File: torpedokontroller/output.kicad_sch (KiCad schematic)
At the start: 17 parts, among them IC9 TCAN3414DR, Q6 PMOS, Q8 STANDARD_140356145200, U3 TPS26400PWP

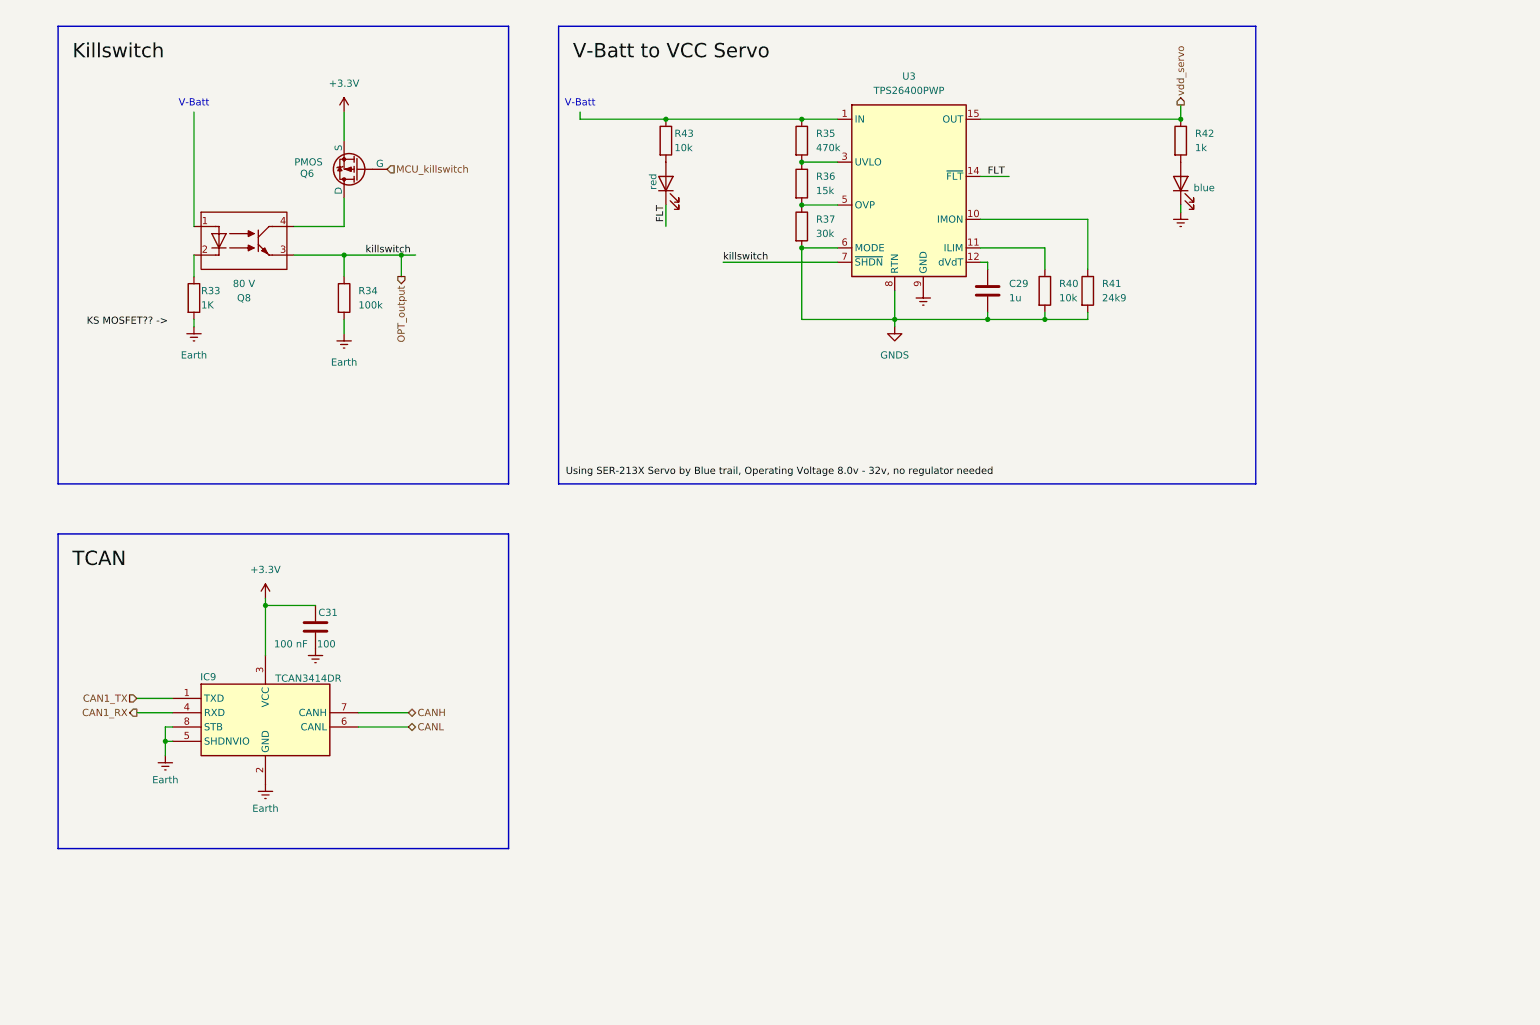
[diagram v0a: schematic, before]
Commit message: v0.5
USB2.0 implemented fr
many other things
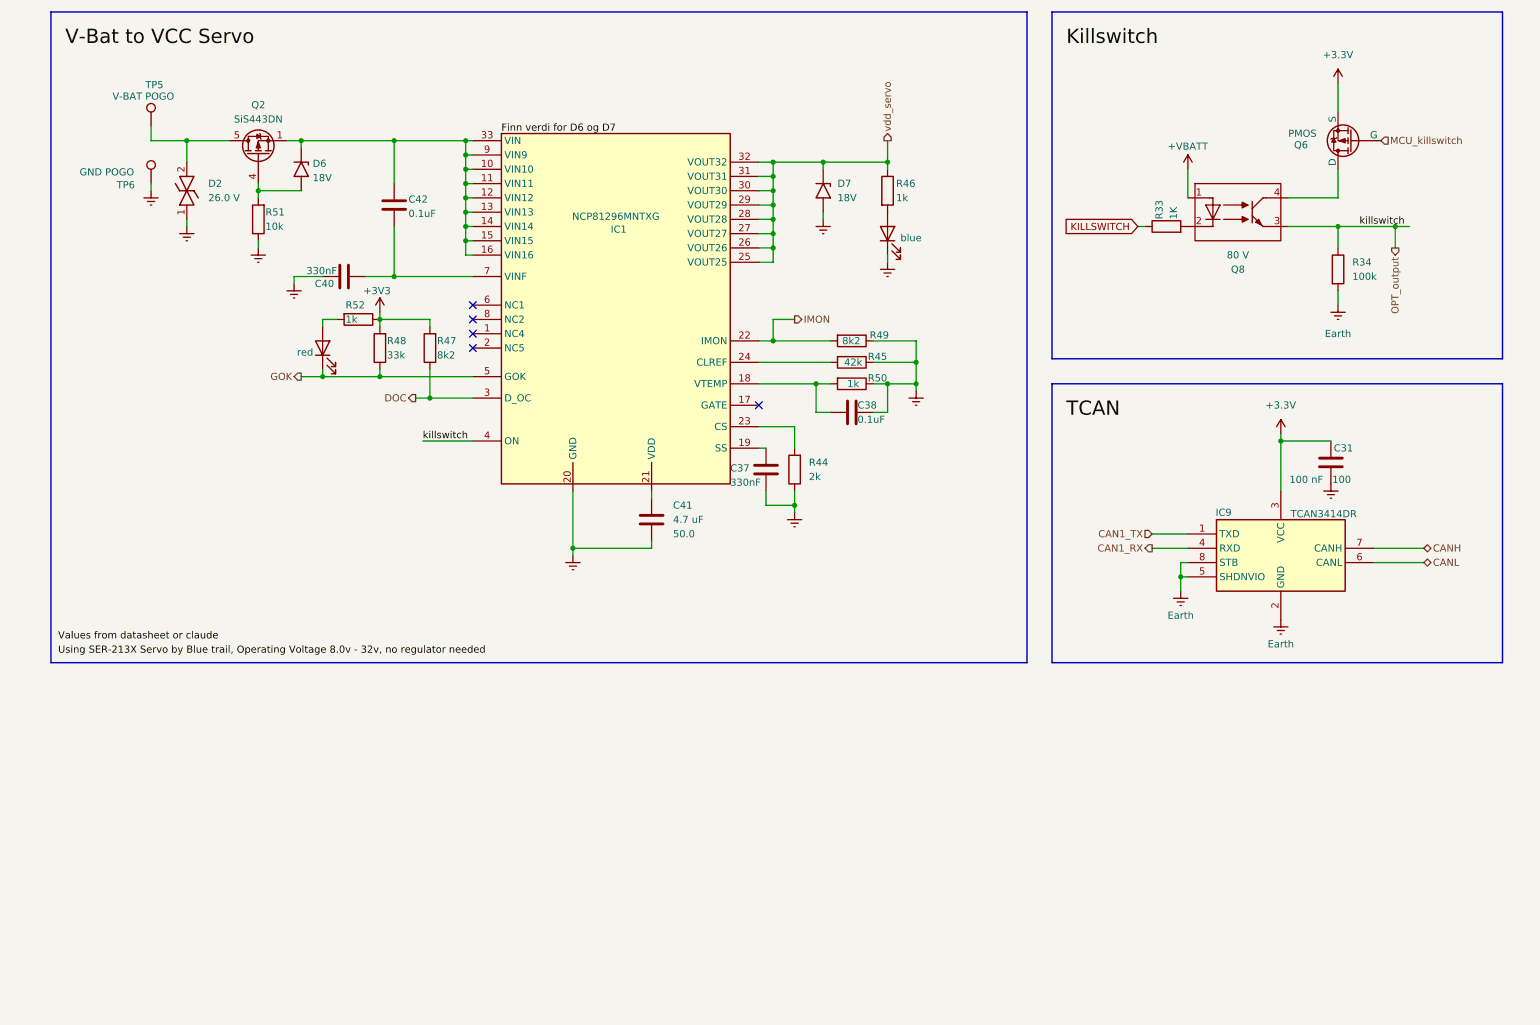
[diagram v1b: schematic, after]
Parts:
- removed C29: 1u, symbol Device:C
- removed D14: blue, symbol Device:LED
- removed D15: red, symbol Device:LED
- removed R35: 470k, symbol Device:R
- removed R36: 15k, symbol Device:R
- removed R37: 30k, symbol Device:R
- removed R40, R43: 10k, symbol Device:R
- removed R41: 24k9, symbol Device:R
- removed R42: 1k, symbol Device:R
- removed U3: TPS26400PWP, Package_SO:HTSSOP-16-1EP_4.4x5mm_P0.65mm_EP3.4x5mm_Mask2.66x2.46mm_ThermalVias, symbol Power_Management:TPS26400PWP
- added C37, C40: 330nF, symbol Device:C
- added C38, C42: 0.1uF, symbol Device:C
- added C41: 4.7 uF, Capacitor_SMD_Wurth:C_Wurth_WCAP-CSGP-1210_H2.5, symbol Capacitor_Wurth_WCAP-CSGP:1210_H2.5_885012209048
- added D16: blue, symbol Device:LED
- added D17: red, symbol Device:LED
- added D2: DO214-AA-600W_BI_824521261, Diode_SMD_Wurth:D_Wurth_WE-TVSP-DO214-AA-600W_BI, symbol WE-TVSP:DO214-AA-600W_BI_824521261
- added D6, D7: 18V, Diode_SMD:D_SMA, symbol Diode:SMAJ18A
- added IC1: NCP81296MNTXG, QFN50P500X500X140-33N, symbol efuse_big:NCP81296MNTXG
- added Q2: SiS443DN, Package_SO:Vishay_PowerPAK_1212-8_Single, symbol Transistor_FET:SiS443DN
- added R44: 2k, symbol Device:R
- added R45: 42k, symbol Device:R
- added R46, R50, R52: 1k, symbol Device:R
- added R47, R49: 8k2, symbol Device:R
- added R48: 33k, symbol Device:R
- added R51: 10k, symbol Device:R
- added TP5: V-BAT POGO, Optocoupler_SMD_Wurth:Q_Wurth_WL-OCPT_SOP4-STANDARD, symbol Connector:TestPoint
- added TP6: GND POGO, Optocoupler_SMD_Wurth:Q_Wurth_WL-OCPT_SOP4-STANDARD, symbol Connector:TestPoint
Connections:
- net Earth: now also C37.2, C38.1, C40.1, C41.2, D16.1 (K), D2.1, D7.2 (A2), IC1.20 (GND), R44.1, R45.1, R49.1, R50.1, R51.1, TP6.1; no longer R33.2
- net OPT_output: now also IC1.4 (ON)
- net vdd_servo: now also D7.1 (A1), IC1.25 (VOUT25), IC1.26 (VOUT26), IC1.27 (VOUT27), IC1.28 (VOUT28), IC1.29 (VOUT29), IC1.30 (VOUT30), IC1.31 (VOUT31), IC1.32 (VOUT32), R46.1
- net +VBATT: now reaches Q8.1 (A)
- net at Q8.2 (C): now also R33.2; no longer R33.1
- new net: IC1.24 (CLREF), R45.2
- new net: D17.2 (A), R52.2
- new net: IC1.23 (CS), R44.2
- new net: C42.2, D6.1 (A1), IC1.10 (VIN10), IC1.11 (VIN11), IC1.12 (VIN12), IC1.13 (VIN13), IC1.14 (VIN14), IC1.15 (VIN15), IC1.16 (VIN16), IC1.33 (VIN), IC1.9 (VIN9), Q2.1 (S), Q2.2 (S), Q2.3 (S)
- new net: D6.2 (A2), Q2.4 (G), R51.2
- new net: D2.2, Q2.5 (D), TP5.1
- new net: D16.2 (A), R46.2
- new net: C41.1, IC1.21 (VDD)
- new net: C37.1, IC1.19 (SS)
- new net: C38.2, IC1.18 (VTEMP), R50.2
- new net: C40.2, C42.1, IC1.7 (VINF)
- new net +3V3: R47.2, R48.2, R52.1
- new net DOC: IC1.3 (D_OC), R47.1
- new net GOK: D17.1 (K), IC1.5 (GOK), R48.1
- new net IMON: IC1.22 (IMON), R49.2
- new net KILLSWITCH: R33.1
- no-connect marks 0 -> 5
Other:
- note removed: "V-Batt"
- moved on the sheet: C31, IC9, Q6, Q8, R33, R34

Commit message: v 0.6
New MCU package
Added SWD, Rest and boot
Moved USB2.0 to MCU page
Other small changes
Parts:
- R49: value 8k2 -> 2k
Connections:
- net DOC renamed D_OC
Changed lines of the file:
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@@
 	(paper "A4")
 	(title_block
-		(date "2026-10-03")
+		(date "2026-10-07")
 		(comment 1 "Simon Torvund")
 	)
@@
 	)
 	(junction
-		(at 146.05 74.93)
+		(at 147.32 74.93)
 		(diameter 0)
 		(color 0 0 0 0)
@@
 	(wire
 		(pts
-			(xy 143.51 74.93) (xy 146.05 74.93)
+			(xy 143.51 74.93) (xy 156.21 74.93)
 		)
 		(stroke
@@
 	(wire
 		(pts
-			(xy 149.86 104.14) (xy 149.86 105.41)
+			(xy 149.86 104.14) (xy 149.86 113.03)
 		)
 		(stroke
@@
 	(wire
 		(pts
-			(xy 146.05 71.12) (xy 149.86 71.12)
+			(xy 147.32 71.12) (xy 151.13 71.12)
 		)
 		(stroke
@@
 	(wire
 		(pts
-			(xy 146.05 74.93) (xy 156.21 74.93)
-		)
-		(stroke
-			(width 0)
-			(type default)
-		)
-	)
-	(wire
-		(pts
 			(xy 166.37 59.69) (xy 166.37 60.96)
 		)
@@
 	(wire
 		(pts
-			(xy 41.91 53.34) (xy 41.91 54.61)
-		)
-		(stroke
-			(width 0)
-			(type default)
-		)
-	)
-	(wire
-		(pts
 			(xy 91.44 41.91) (xy 92.71 41.91)
 		)
@@
 	(wire
 		(pts
-			(xy 146.05 71.12) (xy 146.05 74.93)
+			(xy 147.32 71.12) (xy 147.32 74.93)
 		)
 		(stroke
@@
 	(wire
 		(pts
+			(xy 41.91 53.34) (xy 41.91 58.42)
+		)
+		(stroke
+			(width 0)
+			(type default)
+		)
+	)
+	(wire
+		(pts
 			(xy 78.74 39.37) (xy 91.44 39.37)
 		)
@@
 		)
 	)
-	(label "Values from datasheet or claude"
+	(label "Values from datasheet and claude"
 		(at 19.05 128.27 0)
 		(effects
@@
 		)
 	)
-	(hierarchical_label "DOC"
+	(hierarchical_label "D_OC"
 		(shape output)
 		(at 82.55 85.09 180)
@@
 	(hierarchical_label "IMON"
 		(shape output)
-		(at 149.86 71.12 0)
+		(at 151.13 71.12 0)
 		(effects
 			(font
@@
 			)
 		)
-		(property "Value" "8k2"
+		(property "Value" "2k"
 			(at 161.544 74.93 90)
 			(show_name no)
@@
 	(symbol
 		(lib_id "power:Earth")
-		(at 41.91 54.61 0)
+		(at 41.91 58.42 0)
 		(unit 1)
 		(body_style 1)
@@
 		(fields_autoplaced yes)
 		(property "Reference" "#PWR025"
-			(at 41.91 60.96 0)
+			(at 41.91 64.77 0)
 			(hide yes)
 			(show_name no)
@@
 		)
 		(property "Value" "Earth"
-			(at 41.91 59.69 0)
+			(at 41.91 63.5 0)
 			(hide yes)
 			(show_name no)
@@
 		)
 		(property "Footprint" ""
-			(at 41.91 54.61 0)
+			(at 41.91 58.42 0)
 			(hide yes)
 			(show_name no)
@@
 		)
 		(property "Datasheet" ""
-			(at 41.91 54.61 0)
+			(at 41.91 58.42 0)
 			(hide yes)
 			(show_name no)
@@
 		)
 		(property "Description" "Power symbol creates a global label with name \"Earth\""
-			(at 41.91 54.61 0)
+			(at 41.91 58.42 0)
 			(hide yes)
 			(show_name no)
@@
 	(symbol
 		(lib_id "power:Earth")
-		(at 149.86 105.41 0)
+		(at 149.86 113.03 0)
 		(unit 1)
 		(body_style 1)
@@
 		(fields_autoplaced yes)
 		(property "Reference" "#PWR037"
-			(at 149.86 111.76 0)
+			(at 149.86 119.38 0)
 			(hide yes)
 			(show_name no)
@@
 		)
 		(property "Value" "Earth"
-			(at 149.86 110.49 0)
+			(at 149.86 118.11 0)
 			(hide yes)
 			(show_name no)
@@
 		)
 		(property "Footprint" ""
-			(at 149.86 105.41 0)
+			(at 149.86 113.03 0)
 			(hide yes)
 			(show_name no)
@@
 		)
 		(property "Datasheet" ""
-			(at 149.86 105.41 0)
+			(at 149.86 113.03 0)
 			(hide yes)
 			(show_name no)
@@
 		)
 		(property "Description" "Power symbol creates a global label with name \"Earth\""
-			(at 149.86 105.41 0)
+			(at 149.86 113.03 0)
 			(hide yes)
 			(show_name no)
@@
 		(dnp no)
 		(property "Reference" "C38"
-			(at 161.036 86.36 90)
+			(at 161.544 86.36 90)
 			(show_name no)
 			(do_not_autoplace no)
@@
 		)
 		(property "Value" "0.1uF"
-			(at 161.036 88.9 90)
+			(at 161.544 88.9 90)
 			(show_name no)
 			(do_not_autoplace no)

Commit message: v 0.7
fiksa ting la til ting fjerna ting
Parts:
- removed D7: 18V, Diode_SMD:D_SMA, symbol Diode:SMAJ18A
- added D12, D18: WE-VE_0603, WE-VE_0603:WE-VE_0603, symbol WE-VE_0603:WE-VE_0603
- added D8: DO214-AA-600W_BI_824521261, Diode_SMD_Wurth:D_Wurth_WE-TVSP-DO214-AA-600W_BI, symbol WE-TVSP:DO214-AA-600W_BI_824521261
- added J1: 64900411122, Connector_THT_Wurth:J_Wurth_WR-MPC4_64900411122, symbol WR-MPC4:64900411122
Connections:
- net +3.3V is gone; now on net +3V3: C31.1, IC9.3 (VCC), Q6.3 (S)
- net CANH: now also D18.1, J1.2
- net CANL: now also D12.1, J1.3
- net Earth: now also D12.2, D18.2, D8.1, J1.4
- net 3V3_KS: now reaches Q6.1 (D), Q8.4 (C)
- net vdd_servo renamed VDD_servo
- net VDD_servo: now also D8.2, J1.1
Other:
- moved on the sheet: C31, C37, C38, C40, IC9, Q6, Q8, R33, R34, R44, R45, R46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

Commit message: v 0.8
Fixed one billion things
tvs
many values
connections
cleaned up
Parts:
- removed D16: blue, symbol Device:LED
- removed D17: red, symbol Device:LED
- removed D6: 18V, Diode_SMD:D_SMA, symbol Diode:SMAJ18A
- added D14: 0603_150060BS55040, LED_SMD_Wurth:D_Wurth_WL-SMCD-0603, symbol WL-SMCD:0603_150060BS55040
- added D15: 0603_150060RS55040, LED_SMD_Wurth:D_Wurth_WL-SMCD-0603, symbol WL-SMCD:0603_150060RS55040
- added D17: 12V, Diode_SMD:D_SOD-323, symbol Diode:BZX384xxxx
- added R55, R56: 120, symbol Device:R
- added R58: 1, symbol Device:R
- R46: value 1k -> 4k7
- R52: value 1k -> 160
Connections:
- net +VBATT: now also C42.2, IC1.10 (VIN10), IC1.11 (VIN11), IC1.12 (VIN12), IC1.13 (VIN13), IC1.14 (VIN14), IC1.15 (VIN15), IC1.16 (VIN16), IC1.33 (VIN), IC1.9 (VIN9), Q2.1 (S), Q2.2 (S), Q2.3 (S), D17.1 (K), R58.2
- net CANH: now also R55.1; no longer IC9.7 (CANH)
- net CANL: now also R56.1; no longer IC9.6 (CANL)
- net Earth: now also C42.1, D14.1 (-)
- net GOK: now also D15.1 (-)
- net at R52.2: now also D15.2 (+)
- net at Q2.4 (G), R51.2: now also D17.2 (A)
- net at R46.2: now also D14.2 (+)
- net at C40.2, IC1.7 (VINF): now also R58.1; no longer C42.1
- net MCU_killswitch renamed MCU_KillSwitch
- net OPT_output renamed killswitch
- new net: IC9.7 (CANH), R55.2
- new net: IC9.6 (CANL), R56.2
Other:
- note added: "Killswitch"
- note added: "Servo connector"
- note added: "TCAN"
- note added: "Using SER-213X Servo by Blue trail, Operating Voltage 8.0v - 32v, no regulator needed"
- note added: "V-BAT TO VCC SERVO"
- note added: "Values from datasheet and claude"
- moved on the sheet: C40, C42, R47, R48, R51, R52

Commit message: v 0.9
vet ikke
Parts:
- removed D17: 12V, Diode_SMD:D_SOD-323, symbol Diode:BZX384xxxx
- added D19: 18V, Diode_SMD:D_SMA, symbol Diode:SMAJ18A
- added Z1: 12V, SOD3716X125N, symbol BZT52C10:BZT52C10
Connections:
- net +VBATT: now also Z1.1 (K)
- net Earth: now also D19.2 (A2)
- net VDD_servo: now also D19.1 (A1)
- net at Q2.4 (G), R51.2: now also Z1.2 (A)
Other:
- note added: "Values from datasheet"
- moved on the sheet: C31, IC9, J1, R51, R55, R56, R58

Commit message: v 1.0
Ferdigish

CAN tvs-packages
Ground hook
Test pads
fixed some i/o issues
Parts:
- removed D12, D18: WE-VE_0603, WE-VE_0603:WE-VE_0603, symbol WE-VE_0603:WE-VE_0603
- added D17: SOT23-3L_824094024, Diode_SMD_Wurth:D_Wurth_WE-TVS-SOT23-3L, symbol Diode_Wurth_WE-TVSP:SOT23-3L_824094024
- added J7: H, Connector_THT_Wurth:J_Wurth_WR-PHD_61300111121, symbol Connector_Wurth_WR-PHD:61300111121
- added J8: L, Connector_THT_Wurth:J_Wurth_WR-PHD_61300111121, symbol Connector_Wurth_WR-PHD:61300111121
- added TP10, TP11, TP12, TP9: TestPoint, TestPoint:TestPoint_Pad_D1.5mm, symbol Connector:TestPoint
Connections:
- net CANH: now also D17.1 (I/O1), J7.1
- net CANL: now also D17.2 (I/O2), J8.1
- net D_OC: now also TP10.1
- net Earth: now also D17.3 (GND)
- net GOK: now also TP9.1
- net IMON: now also TP11.1
- net MCU_KillSwitch: now also TP12.1
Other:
- moved on the sheet: C38, D15, D19, D8, J1, R45, R47, R48, R49, R50, R52

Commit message: some footprints + print
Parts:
- removed C40: 330nF, symbol Device:C
- removed Q8: STANDARD_140356145200, Optocoupler_SMD_Wurth:Q_Wurth_WL-OCPT_SOP4-STANDARD, symbol WL-OCPT SOP-4:STANDARD_140356145200
- added C46: 10nF, Capasitors:C_Wurth_WCAP-CSGP-0603_R, symbol Device:C
- added Q1: STANDARD_140356145200, WL-OCPT:Q_Wurth_WL-OCPT_SOP4-STANDARD, symbol WL-OCPT SOP-4:STANDARD_140356145200
- C31, C41: footprint Capacitor_SMD_Wurth:C_Wurth_WCAP-CSGP-1210_H2.5 -> Capasitors:C_Wurth_WCAP-CSGP-0603_R
- C37, C38, C42: footprint (none) -> Capasitors:C_Wurth_WCAP-CSGP-0603_R
- D14, D15: footprint LED_SMD_Wurth:D_Wurth_WL-SMCD-0603 -> WL-LED:D_Wurth_WL-SMCD-0603
- D17: footprint Diode_SMD_Wurth:D_Wurth_WE-TVS-SOT23-3L -> Package_TO_SOT_SMD:SOT-23-3
- D2, D8: footprint Diode_SMD_Wurth:D_Wurth_WE-TVSP-DO214-AA-600W_BI -> Diode_SMD:D_SMB
- IC1: footprint QFN50P500X500X140-33N -> (none)
- R33, R34, R44, R45, R46, R47, R48, R49, R50, R51, R52, R55, R56: footprint (none) -> WE-Resistors:R_Wurth_WRIS-KSKE-0603
- R58: value 1 -> 10; footprint (none) -> WE-Resistors:R_Wurth_WRIS-KSKE-0603
- Z1: footprint SOD3716X125N -> (none)
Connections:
- net +VBATT: now also Q1.1 (A)
- net 3V3_KS: now also Q1.4 (C)
- net Earth: now also C46.1
- net killswitch: now also Q1.3 (E)
- net at R33.2: now also Q1.2 (C)
- net at IC1.7 (VINF), R58.1: now also C46.2

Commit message: v 1.1
Fiksa ting
starta layout
bedre schematic design
whooppppppwhhoop
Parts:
- removed D2, D8: DO214-AA-600W_BI_824521261, Diode_SMD:D_SMB, symbol WE-TVSP:DO214-AA-600W_BI_824521261
- removed TP10, TP9: TestPoint, TestPoint:TestPoint_Pad_D1.5mm, symbol Connector:TestPoint
- removed TP5: V-BAT POGO, Optocoupler_SMD_Wurth:Q_Wurth_WL-OCPT_SOP4-STANDARD, symbol Connector:TestPoint
- removed TP6: GND POGO, Optocoupler_SMD_Wurth:Q_Wurth_WL-OCPT_SOP4-STANDARD, symbol Connector:TestPoint
- removed Z1: 12V, symbol BZT52C10:BZT52C10
- added D5: DFN1610-2L_824045817, Diode_SMD_Wurth:D_Wurth_WE-TVS-DFN1610-2L, symbol Diode_Wurth_WE-TVSP:DFN1610-2L_824045817
- IC1: footprint (none) -> big_efuse:QFN50P500X500X140-33N
- J1: footprint Connector_THT_Wurth:J_Wurth_WR-MPC4_64900411122 -> Connectors_tht:J_Wurth_WR-MPC4_64900411122
- J7, J8: footprint Connector_THT_Wurth:J_Wurth_WR-PHD_61300111121 -> Connectors_tht:J_Wurth_WR-PHD_61300111121
- Q6: footprint Package_DIP:DIP-24_W7.62mm -> (none)
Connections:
- net at Q2.4 (G), R51.2: now also D5.2 (GND)
- net VBAT-CON: now reaches Q2.5 (D)
- net +VBATT renamed +VBAT
- net +VBAT: now also D5.1 (I/O)
- net VDD_servo renamed +VDD_servo
